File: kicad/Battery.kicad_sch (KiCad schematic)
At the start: 62 parts, among them Q1 FMMT493, Q2 AO3400A, Q3 AO3400A, U7 S5B-XH-A(LF)(SN), U8 XT30PW-M, U9 BQ7694202PFBR

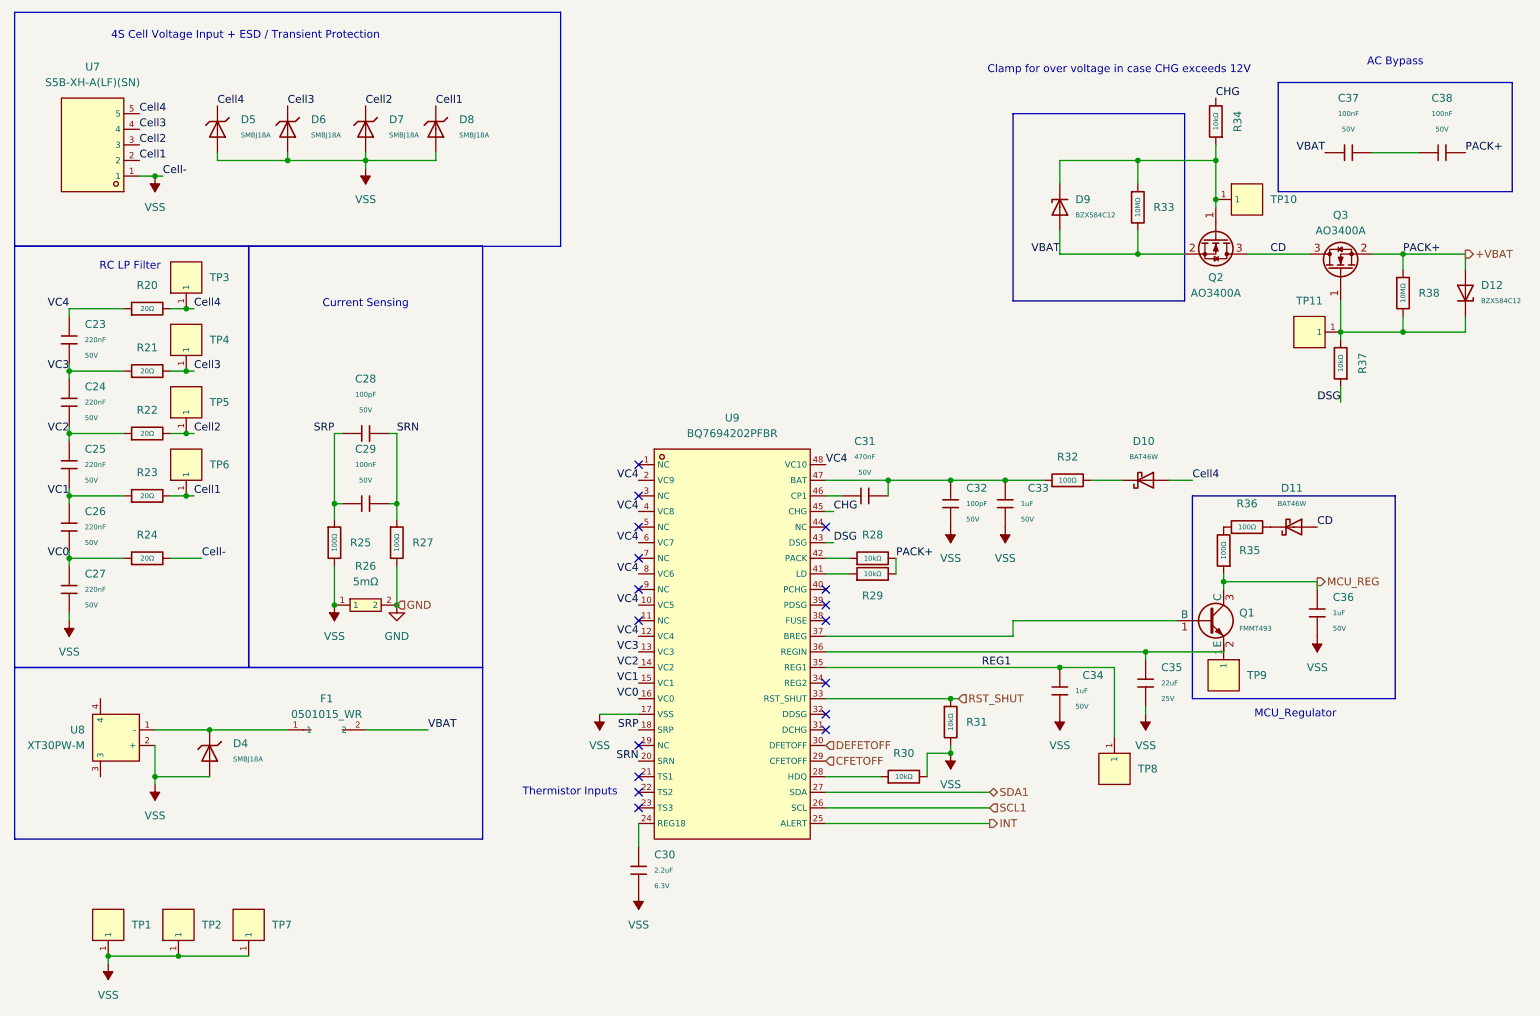
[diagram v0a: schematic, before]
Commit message: Charger IC footprint routed RP2040 routed BMS routed xt30s and balancers router
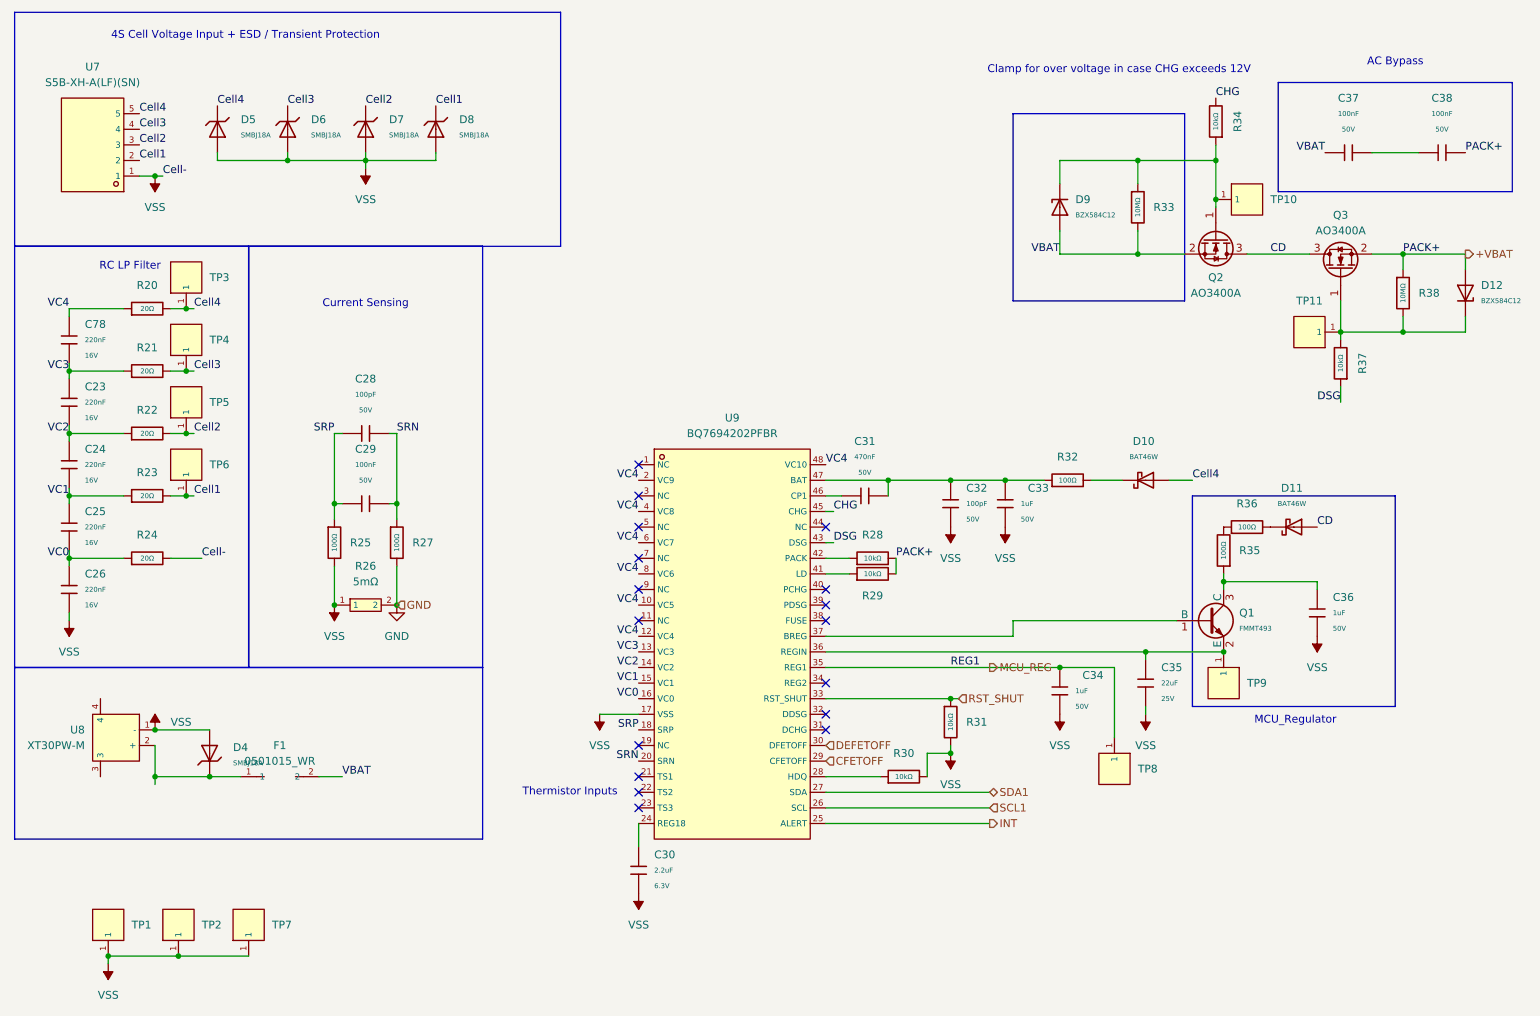
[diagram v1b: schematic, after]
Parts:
- removed C23, C24, C25, C26, C27: 220nF, PCM_JLCPCB:C_0805, symbol PCM_JLCPCB-Capacitors:0805,220nF
- added C23, C24, C25, C26, C78: 220nF, PCM_JLCPCB:C_0402, symbol PCM_JLCPCB-Capacitors:0402,220nF
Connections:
- net REG1 is gone; now on net MCU_REG: C34.1, TP8.1, U9.35 (REG1)
- net MCU_REG: no longer C36.1, Q1.3 (C), R35.1
- net VC0: now also C25.2, C26.1
- net VC1: now also C24.2, C25.1
- net VC2: now also C23.2, C24.1
- net VC3: now also C23.1, C78.2
- net VC4: now also C78.1
- net VSS: now also U8.1 (-), C26.2; no longer U8.2 (+)
- net at TP9.1: now also C35.1, Q1.2 (E), U9.36 (REGIN)
- net at D4.1, F1.1: now also U8.2 (+); no longer U8.1 (-)
- new net: C36.1, Q1.3 (C), R35.1
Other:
- moved on the sheet: D4, F1, TP9

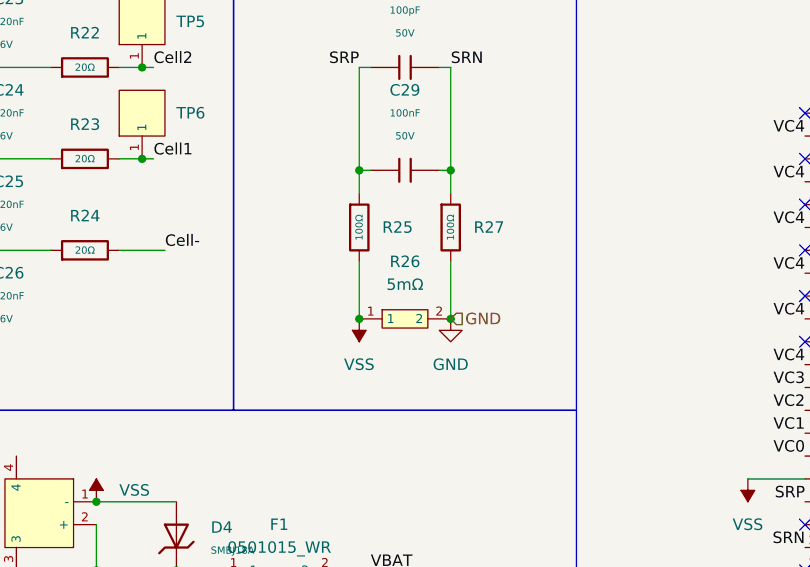
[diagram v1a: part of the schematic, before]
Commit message: Replace R26 with R1206 footprint and update PCB
Replaced the R26 resistor from an R0805 to an R1206 footprint in the PCB layout and netlist, updated associated tracks and vias, and added the new R1206 footprint file. Updated schematic, BOM, designators, and positions to reflect this change. Cleaned up related net connections and removed the old R0805 instance.
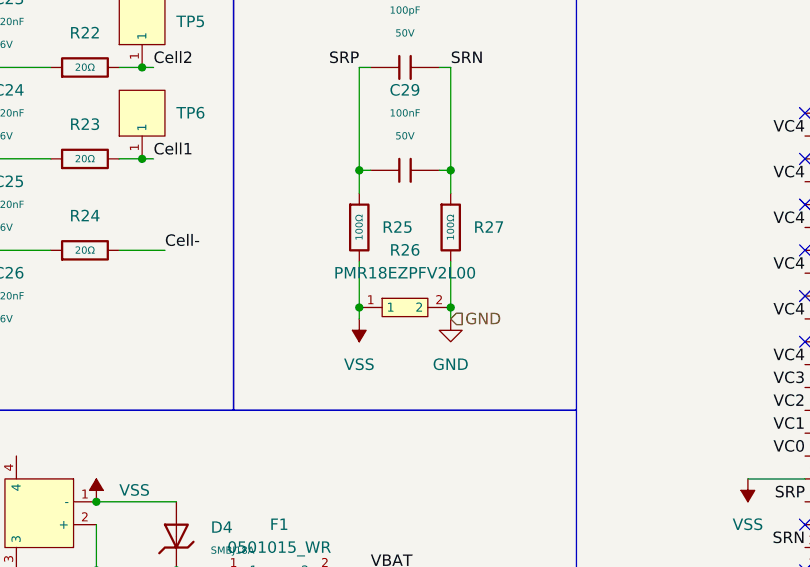
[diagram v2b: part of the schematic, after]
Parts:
- removed R26: 5mΩ, 4in-power:R0805, symbol 4in-power:MS05W2F500NT5E
- added R26: PMR18EZPFV2L00, 4in-power:R1206, symbol 4in-power:PMR18EZPFV2L00
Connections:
- net GND: now also R26.2
- net VSS: now also R26.1
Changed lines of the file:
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@@
 	)
 	(junction
-		(at 198.12 116.84)
+		(at 66.04 107.95)
 		(diameter 0)
 		(color 0 0 0 0)
 	)
 	(junction
-		(at 210.82 105.41)
+		(at 198.12 116.84)
 		(diameter 0)
 		(color 0 0 0 0)
 	)
 	(junction
-		(at 76.2 109.22)
+		(at 210.82 105.41)
 		(diameter 0)
 		(color 0 0 0 0)
@@
 	)
 	(junction
+		(at 76.2 107.95)
+		(diameter 0)
+		(color 0 0 0 0)
+	)
+	(junction
 		(at 22.86 81.28)
 		(diameter 0)
@@
 	)
 	(junction
-		(at 66.04 109.22)
-		(diameter 0)
-		(color 0 0 0 0)
-	)
-	(junction
 		(at 175.26 88.9)
 		(diameter 0)
@@
 	(wire
 		(pts
-			(xy 66.04 102.87) (xy 66.04 109.22)
+			(xy 66.04 102.87) (xy 66.04 107.95)
 		)
 		(stroke
@@
 	(wire
 		(pts
+			(xy 76.2 107.95) (xy 76.2 109.22)
+		)
+		(stroke
+			(width 0)
+			(type default)
+		)
+	)
+	(wire
+		(pts
 			(xy 250.19 64.77) (xy 240.03 64.77)
 		)
@@
 	(wire
 		(pts
-			(xy 76.2 102.87) (xy 76.2 109.22)
+			(xy 76.2 102.87) (xy 76.2 107.95)
 		)
 		(stroke
@@
 	(wire
 		(pts
+			(xy 66.04 107.95) (xy 66.04 109.22)
+		)
+		(stroke
+			(width 0)
+			(type default)
+		)
+	)
+	(wire
+		(pts
 			(xy 162.56 133.35) (xy 166.37 133.35)
 		)
@@
 	)
 	(symbol
+		(lib_id "4in-power:PMR18EZPFV2L00")
+		(at 71.12 107.95 0)
+		(unit 1)
+		(exclude_from_sim no)
+		(in_bom yes)
+		(on_board yes)
+		(dnp no)
+		(fields_autoplaced yes)
+		(property "Reference" "R26"
+			(at 71.12 101.6 0)
+			(effects
+				(font
+					(size 1.27 1.27)
+				)
+			)
+		)
+		(property "Value" "PMR18EZPFV2L00"
+			(at 71.12 104.14 0)
+			(effects
+				(font
+					(size 1.27 1.27)
+				)
+			)
+		)
+		(property "Footprint" "4in-power:R1206"
+			(at 71.12 118.11 0)
+			(effects
+				(font
+					(size 1.27 1.27)
+					(italic yes)
+				)
+				(hide yes)
+			)
+		)
+		(property "Datasheet" "https://item.szlcsc.com/311874.html"
+			(at 68.834 107.823 0)
+			(effects
+				(font
+					(size 1.27 1.27)
+				)
+				(justify left)
+				(hide yes)
+			)
+		)
+		(property "Description" ""
+			(at 71.12 107.95 0)
+			(effects
+				(font
+					(size 1.27 1.27)
+				)
+				(hide yes)
+			)
+		)
+		(property "LCSC" "C92124"
+			(at 71.12 107.95 0)
+			(effects
+				(font
+					(size 1.27 1.27)
+				)
+				(hide yes)
+			)
+		)
+		(pin "2"
+		)
+		(pin "1"
+		)
+		(instances
+			(project ""
+				(path "/612ece3f-e722-4b33-8111-645d24cfcf05/b5ab9921-5796-498c-b0d6-2d1294fdeff4/edeeb5f2-16ab-4212-91f0-b72c52b2aaa4"
+					(reference "R26")
+					(unit 1)
+				)
+			)
+		)
+	)
+	(symbol
 		(lib_id "4in-power:RH-5015")
 		(at 41.91 66.04 90)
@@
 					(unit 1)
 				)
-			)
-		)
-	)
-	(symbol
-		(lib_id "4in-power:MS05W2F500NT5E")
-		(at 71.12 109.22 0)
-		(unit 1)
-		(exclude_from_sim no)
-		(in_bom yes)
-		(on_board yes)
-		(dnp no)
-		(fields_autoplaced yes)
-		(property "Reference" "R26"
-			(at 71.12 102.87 0)
-			(effects
-				(font
-					(size 1.27 1.27)
-				)
-			)
-		)
-		(property "Value" "5mΩ"
-			(at 71.12 105.41 0)
-			(effects
-				(font
-					(size 1.27 1.27)
-				)
-			)
-		)
-		(property "Footprint" "4in-power:R0805"
-			(at 71.12 119.38 0)
-			(effects
-				(font
-					(size 1.27 1.27)
-					(italic yes)
-				)
-				(hide yes)
-			)
-		)
-		(property "Datasheet" "https://item.szlcsc.com/142685.html"
-			(at 68.834 109.093 0)
-			(effects
-				(font
-					(size 1.27 1.27)
-				)
-				(justify left)
-				(hide yes)
-			)
-		)
-		(property "Description" "500mW 5mΩ Current Sense Resistor Surface Mount ±1% ±150ppm/℃ 0805 Current Sense Resistors / Shunt Resistors ROHS"
-			(at 71.12 109.22 0)
-			(effects
-				(font
-					(size 1.27 1.27)
-				)
-				(hide yes)
-			)
-		)
-		(property "LCSC" "C92742"
-			(at 71.12 109.22 0)
-			(effects
-				(font
-					(size 1.27 1.27)
-				)
-				(hide yes)
-			)
-		)
-		(property "MFR PART #" "MS05W2F500NT5E"
-			(at 71.12 109.22 0)
-			(effects
-				(font
-					(size 1.27 1.27)
-				)
-				(hide yes)
-			)
-		)
-		(pin "2"
-		)
-		(pin "1"
-		)
-		(instances
-			(project "4-in-power-improved"
-				(path "/612ece3f-e722-4b33-8111-645d24cfcf05/b5ab9921-5796-498c-b0d6-2d1294fdeff4/edeeb5f2-16ab-4212-91f0-b72c52b2aaa4"
-					(reference "R26")
-					(unit 1)
-				)
